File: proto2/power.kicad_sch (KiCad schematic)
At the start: 27 parts, among them Q15 2N7002, Q16 AO3401A

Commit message: Final layout for 0.2.0 and various BOM and minor schematic updates.
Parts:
- added R158: 1K, Resistor_SMD:R_0805_2012Metric, symbol Device:R_Small
- C52, C53, R149, R19, R20, R53, R54, R59: Config DNP -> (none); MPN (none) -> DNP
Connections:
- net at Q15.1 (G), R55.1, R56.1: now also R158.1
- new net +3V3: R158.2
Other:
- note added: "DNP: R149"
- note added: "DNP: R54 R59"
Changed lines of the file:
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@@
   (junction (at 97.79 44.45) (diameter 0) (color 0 0 0 0)
   )
+  (junction (at 80.01 130.81) (diameter 0) (color 0 0 0 0)
+  )
   (junction (at 100.33 44.45) (diameter 0) (color 0 0 0 0)
   )
@@
     (stroke (width 0) (type default) (color 0 0 0 0))
   )
+  (wire (pts (xy 80.01 123.19) (xy 80.01 130.81))
+    (stroke (width 0) (type default) (color 0 0 0 0))
+  )
   (wire (pts (xy 228.6 128.27) (xy 228.6 123.19))
     (stroke (width 0) (type default) (color 0 0 0 0))
@@
     (stroke (width 0) (type default) (color 0 0 0 0))
   )
+  (wire (pts (xy 68.58 123.19) (xy 68.58 121.92))
+    (stroke (width 0) (type default) (color 0 0 0 0))
+  )
   (wire (pts (xy 195.58 52.07) (xy 210.82 52.07))
     (stroke (width 0) (type default) (color 0 0 0 0))
@@
     (stroke (width 0) (type default) (color 0 0 0 0))
   )
-  (wire (pts (xy 77.47 130.81) (xy 81.28 130.81))
+  (wire (pts (xy 77.47 130.81) (xy 80.01 130.81))
     (stroke (width 0) (type default) (color 0 0 0 0))
   )
@@
     (stroke (width 0) (type default) (color 0 0 0 0))
   )
+  (wire (pts (xy 72.39 123.19) (xy 68.58 123.19))
+    (stroke (width 0) (type default) (color 0 0 0 0))
+  )
   (wire (pts (xy 128.27 54.61) (xy 143.51 54.61))
     (stroke (width 0) (type default) (color 0 0 0 0))
@@
     (stroke (width 0) (type default) (color 0 0 0 0))
   )
+  (wire (pts (xy 77.47 123.19) (xy 80.01 123.19))
+    (stroke (width 0) (type default) (color 0 0 0 0))
+  )
   (wire (pts (xy 76.2 52.07) (xy 76.2 54.61))
     (stroke (width 0) (type default) (color 0 0 0 0))
@@
     (stroke (width 0) (type default) (color 0 0 0 0))
   )
+  (wire (pts (xy 80.01 130.81) (xy 81.28 130.81))
+    (stroke (width 0) (type default) (color 0 0 0 0))
+  )
   (wire (pts (xy 86.36 138.43) (xy 91.44 138.43))
     (stroke (width 0) (type default) (color 0 0 0 0))
@@
   (wire (pts (xy 224.79 123.19) (xy 228.6 123.19))
     (stroke (width 0) (type default) (color 0 0 0 0))
+  )
+  (text "DNP:\nR149" (at 138.43 118.11 0)
+    (effects (font (size 1.27 1.27)) (justify left bottom))
   )
   (text "https://electronics.stackexchange.com/questions/19561/should-chassis-ground-be-attached-to-digital-ground"
     (at 302.26 116.84 0)
+    (effects (font (size 1.27 1.27)) (justify left bottom))
+  )
+  (text "DNP:\nR54\nR59" (at 180.34 137.16 0)
     (effects (font (size 1.27 1.27)) (justify left bottom))
   )
@@
       (effects (font (size 1.27 1.27)) hide)
     )
-    (property "Datasheet" "~" (id 3) (at 68.58 44.45 0)
+    (property "Datasheet" "https://datasheet.lcsc.com/lcsc/1810250922_Murata-Electronics-LQH32PN2R2NN0L_C86074.pdf" (id 3) (at 68.58 44.45 0)
       (effects (font (size 1.27 1.27)) hide)
     )
@@
       (effects (font (size 1.27 1.27)) hide)
     )
-    (property "Datasheet" "~" (id 3) (at 46.99 49.53 0)
+    (property "Datasheet" "https://datasheet.lcsc.com/lcsc/1810261813_Honor-Elec-VT1H331M1213_C94443.pdf" (id 3) (at 46.99 49.53 0)
       (effects (font (size 1.27 1.27)) hide)
     )
@@
       (effects (font (size 1.27 1.27)) hide)
     )
-    (property "Datasheet" "~" (id 3) (at 87.63 49.53 0)
+    (property "Datasheet" "https://datasheet.lcsc.com/lcsc/1810261813_Honor-Elec-VT1H331M1213_C94443.pdf" (id 3) (at 87.63 49.53 0)
       (effects (font (size 1.27 1.27)) hide)
     )
@@
       (effects (font (size 1.27 1.27)) hide)
     )
-    (property "Config" "DNP" (id 4) (at 210.82 45.72 0)
+    (property "Config" "" (id 4) (at 210.82 45.72 0)
+      (effects (font (size 1.27 1.27)) hide)
+    )
+    (property "MPN" "DNP" (id 5) (at 210.82 45.72 0)
       (effects (font (size 1.27 1.27)) hide)
     )
@@
       (effects (font (size 1.27 1.27)) hide)
     )
-    (property "Config" "DNP" (id 4) (at 210.82 57.15 0)
+    (property "Config" "" (id 4) (at 210.82 57.15 0)
+      (effects (font (size 1.27 1.27)) hide)
+    )
+    (property "MPN" "DNP" (id 5) (at 210.82 57.15 0)
       (effects (font (size 1.27 1.27)) hide)
     )
@@
       (effects (font (size 1.27 1.27)) hide)
     )
-    (property "Config" "DNP" (id 5) (at 234.95 114.3 90)
+    (property "Config" "" (id 5) (at 234.95 114.3 90)
+      (effects (font (size 1.27 1.27)) hide)
+    )
+    (property "MPN" "DNP" (id 6) (at 234.95 114.3 0)
       (effects (font (size 1.27 1.27)) hide)
     )
@@
       (effects (font (size 1.27 1.27)) hide)
     )
-    (property "Config" "DNP" (id 5) (at 222.25 123.19 0)
+    (property "Config" "" (id 5) (at 222.25 123.19 0)
+      (effects (font (size 1.27 1.27)) hide)
+    )
+    (property "MPN" "DNP" (id 6) (at 222.25 123.19 0)
       (effects (font (size 1.27 1.27)) hide)
     )
@@
       (effects (font (size 1.27 1.27)) hide)
     )
-    (property "Config" "DNP" (id 5) (at 234.95 123.19 0)
+    (property "Config" "" (id 5) (at 234.95 123.19 0)
+      (effects (font (size 1.27 1.27)) hide)
+    )
+    (property "MPN" "DNP" (id 6) (at 234.95 123.19 0)
       (effects (font (size 1.27 1.27)) hide)
     )
@@
       (effects (font (size 1.27 1.27)) hide)
     )
-    (property "Config" "DNP" (id 5) (at 135.89 123.19 0)
+    (property "Config" "" (id 5) (at 135.89 123.19 0)
+      (effects (font (size 1.27 1.27)) hide)
+    )
+    (property "MPN" "DNP" (id 6) (at 135.89 123.19 0)
       (effects (font (size 1.27 1.27)) hide)
     )
@@
     (pin "1")
   )
+  (symbol (lib_id "Device:R_Small") (at 74.93 123.19 270) (unit 1)
+    (in_bom yes) (on_board yes)
+    (property "Reference" "R158" (id 0) (at 74.93 118.2116 90))
+    (property "Value" "1K" (id 1) (at 74.93 120.523 90))
+    (property "Footprint" "Resistor_SMD:R_0805_2012Metric" (id 2) (at 74.93 123.19 0)
+      (effects (font (size 1.27 1.27)) hide)
+    )
+    (property "Datasheet" "https://datasheet.lcsc.com/lcsc/2110251730_UNI-ROYAL-Uniroyal-Elec-0805W8F1001T5E_C17513.pdf" (id 3) (at 74.93 123.19 0)
+      (effects (font (size 1.27 1.27)) hide)
+    )
+    (property "LCSC" "C17513" (id 4) (at 74.93 123.19 0)
+      (effects (font (size 1.27 1.27)) hide)
+    )
+    (property "MPN" "DNP" (id 5) (at 74.93 123.19 0)
+      (effects (font (size 1.27 1.27)) hide)
+    )
+    (pin "1")
+    (pin "2")
+  )
   (symbol (lib_id "power:+5VP") (at 135.89 129.54 180) (unit 1)
     (in_bom yes) (on_board yes) (fields_autoplaced)
@@
   (symbol (lib_id "power:+5V") (at 210.82 40.64 0) (unit 1)
     (in_bom yes) (on_board yes)
-    (property "Reference" "#PWR?" (id 0) (at 210.82 44.45 0)
+    (property "Reference" "#PWR0120" (id 0) (at 210.82 44.45 0)
       (effects (font (size 1.27 1.27)) hide)
     )
@@
     (pin "1")
   )
+  (symbol (lib_id "power:+3.3V") (at 68.58 121.92 0) (unit 1)
+    (in_bom yes) (on_board yes)
+    (property "Reference" "#PWR035" (id 0) (at 68.58 125.73 0)
+      (effects (font (size 1.27 1.27)) hide)
+    )
+    (property "Value" "+3.3V" (id 1) (at 68.961 117.5258 0))
+    (property "Footprint" "" (id 2) (at 68.58 121.92 0)
+      (effects (font (size 1.27 1.27)) hide)
+    )
+    (property "Datasheet" "" (id 3) (at 68.58 121.92 0)
+      (effects (font (size 1.27 1.27)) hide)
+    )
+    (pin "1")
+  )
   (symbol (lib_id "Transistor_FET:AO3401A") (at 118.11 123.19 0) (mirror x) (unit 1)
     (in_bom yes) (on_board yes) (fields_autoplaced)
@@
       (effects (font (size 1.27 1.27)) hide)
     )
-    (property "Config" "DNP" (id 5) (at 171.45 119.38 90)
+    (property "Config" "" (id 5) (at 171.45 119.38 90)
+      (effects (font (size 1.27 1.27)) hide)
+    )
+    (property "MPN" "DNP" (id 6) (at 171.45 119.38 0)
       (effects (font (size 1.27 1.27)) hide)
     )
@@
   (symbol (lib_id "power:+5V") (at 168.91 35.56 0) (unit 1)
     (in_bom yes) (on_board yes)
-    (property "Reference" "#PWR?" (id 0) (at 168.91 39.37 0)
+    (property "Reference" "#PWR0108" (id 0) (at 168.91 39.37 0)
       (effects (font (size 1.27 1.27)) hide)
     )
@@
       (effects (font (size 1.27 1.27)) hide)
     )
-    (property "Config" "DNP" (id 5) (at 171.45 127 90)
-      (effects (font (size 1.27 1.27)) hide)
-    )
+    (property "Config" "" (id 5) (at 171.45 127 90)
+      (effects (font (size 1.27 1.27)) hide)
+    )
+    (property "MPN" "DNP" (id 6) (at 171.45 127 0)
+      (effects (font (size 1.27 1.27)) hide)
+    )

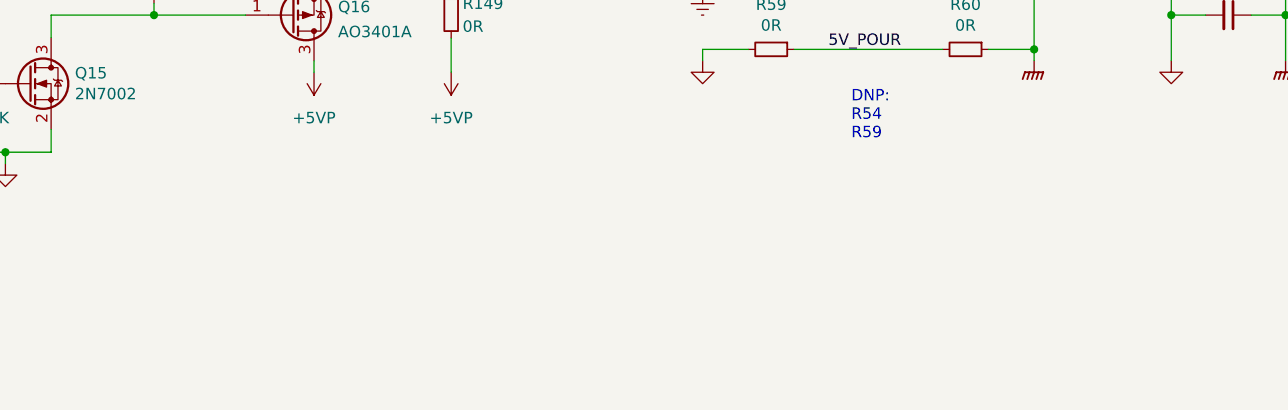
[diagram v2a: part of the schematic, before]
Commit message: Rearranged GPIO around the boot pins.
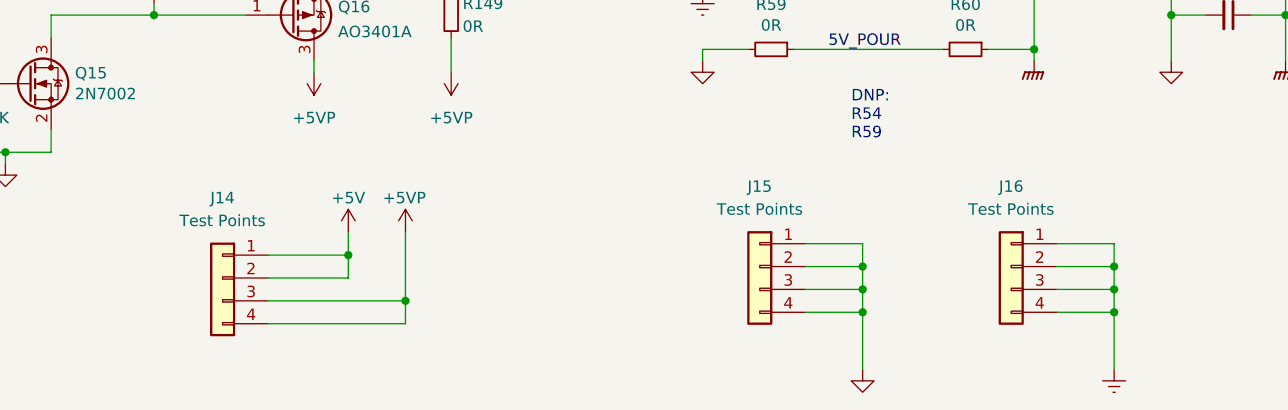
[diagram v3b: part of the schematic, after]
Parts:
- added J14, J15, J16: Test Points, Connector_PinHeader_2.54mm:PinHeader_1x04_P2.54mm_Vertical, symbol Connector_Generic:Conn_01x04
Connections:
- net +5V: now also J14.1 (Pin_1), J14.2 (Pin_2)
- net +5VP: now also J14.3 (Pin_3), J14.4 (Pin_4)
- net GND-PWR: now also J16.1 (Pin_1), J16.2 (Pin_2), J16.3 (Pin_3), J16.4 (Pin_4)
- net GND-SIG: now also J15.1 (Pin_1), J15.2 (Pin_2), J15.3 (Pin_3), J15.4 (Pin_4)

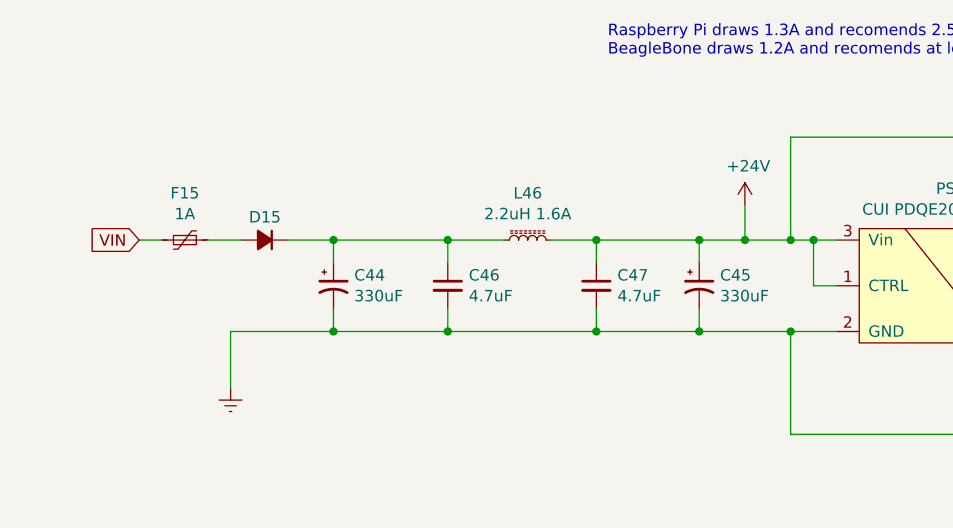
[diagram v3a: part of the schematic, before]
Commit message: Added larger fuse for 24V, replaced main polarity diode, and relayed out board to fit new components.
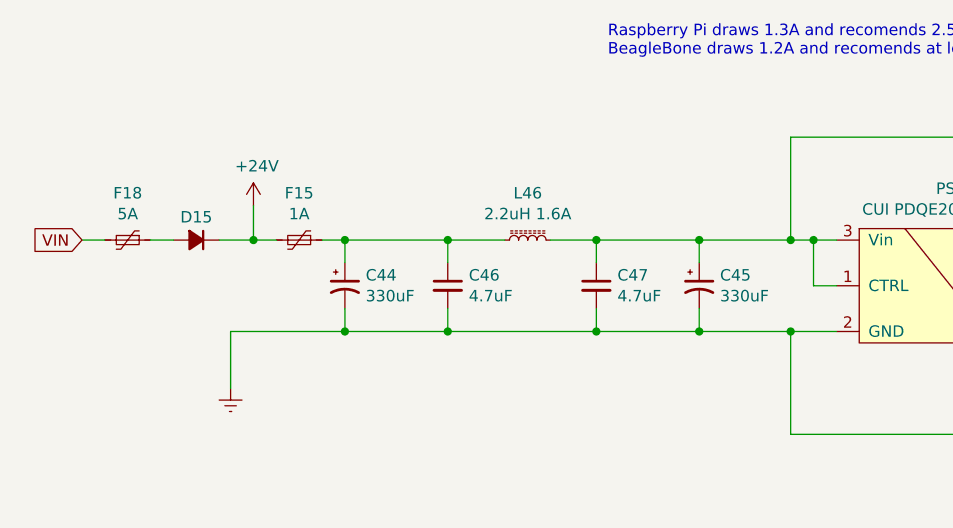
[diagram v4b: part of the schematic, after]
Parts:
- added F18: 5A, JLCPCB:F_2920, symbol Device:Polyfuse_Small
- D15: footprint Diode_SMD:D_SOD-123F -> Diode_SMD:D_SMC; LCSC C64898 -> C335615; Manufacturer MDD -> Vishay; Part Number SM4007PL -> S5JHE3_A/I
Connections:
- net +24V: now also D15.1 (K), F15.2; no longer C43.2, C45.1, C47.1, L46.2, PS1.1 (CTRL), PS1.3 (Vin)
- net VIN: now also F18.2; no longer F15.2
- net at C44.1, C46.1, L46.1: now also F15.1; no longer D15.1 (K)
- net at D15.2 (A): now also F18.1; no longer F15.1
- new net: C43.2, C45.1, C47.1, L46.2, PS1.1 (CTRL), PS1.3 (Vin)
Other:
- moved on the sheet: C44, D15, F15

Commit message: Updated PTC sizes so they will not trip with typical current draw.
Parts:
- F15: footprint Resistor_SMD:R_1206_3216Metric -> JLCPCB:F_2920; LCSC C70077 -> C409807
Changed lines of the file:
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@@
     (property "Reference" "F15" (id 0) (at 43.18 39.243 90))
     (property "Value" "1A" (id 1) (at 43.18 41.5544 90))
-    (property "Footprint" "Resistor_SMD:R_1206_3216Metric" (id 2) (at 38.1 45.72 0)
+    (property "Footprint" "JLCPCB:F_2920" (id 2) (at 38.1 45.72 0)
       (effects (font (size 1.27 1.27)) (justify left) hide)
     )
-    (property "Datasheet" "https://datasheet.lcsc.com/lcsc/1809211126_TECHFUSE-nSMD050-33V_C70077.pdf" (id 3) (at 43.18 44.45 0)
+    (property "Datasheet" "https://datasheet.lcsc.com/lcsc/1912111437_Jinrui-Electronic-Materials-Co--JK-SMD100L_C409807.pdf" (id 3) (at 43.18 44.45 0)
       (effects (font (size 1.27 1.27)) hide)
     )
-    (property "LCSC" "C70077" (id 4) (at 43.18 44.45 0)
+    (property "LCSC" "C409807" (id 4) (at 43.18 44.45 0)
       (effects (font (size 1.27 1.27)) hide)
     )

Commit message: Changed revision on schematic to 0.3.0.
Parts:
- J14, J15, J16, PS1: now left out of the parts list
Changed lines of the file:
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@@
   (title_block
     (title "Greenhouse 2.0 IO Board")
-    (date "2022-06-07")
-    (rev "0.2.1")
+    (date "2022-07-26")
+    (rev "0.3.0")
     (company "Langhe Greenhaus")
     (comment 1 "Langhe Part Number: 240000")
@@
   )
   (symbol (lib_id "BCR:CUI_PDQE20_ISOLATED_DCDC") (at 115.57 49.53 0) (unit 1)
-    (in_bom yes) (on_board yes)
+    (in_bom no) (on_board yes)
     (property "Reference" "PS1" (id 0) (at 115.57 38.735 0))
     (property "Value" "CUI PDQE20-Q24-S5-D" (id 1) (at 115.57 41.0464 0))
@@
   )
   (symbol (lib_id "Connector_Generic:Conn_01x04") (at 170.18 151.13 0) (mirror y) (unit 1)
-    (in_bom yes) (on_board yes) (fields_autoplaced)
+    (in_bom no) (on_board yes) (fields_autoplaced)
     (property "Reference" "J15" (id 0) (at 170.18 142.24 0))
     (property "Value" "Test Points" (id 1) (at 170.18 144.78 0))
@@
   )
   (symbol (lib_id "Connector_Generic:Conn_01x04") (at 110.49 152.4 0) (mirror y) (unit 1)
-    (in_bom yes) (on_board yes) (fields_autoplaced)
+    (in_bom no) (on_board yes) (fields_autoplaced)
     (property "Reference" "J14" (id 0) (at 110.49 143.51 0))
     (property "Value" "Test Points" (id 1) (at 110.49 146.05 0))
@@
   )
   (symbol (lib_id "Connector_Generic:Conn_01x04") (at 198.12 151.13 0) (mirror y) (unit 1)
-    (in_bom yes) (on_board yes) (fields_autoplaced)
+    (in_bom no) (on_board yes) (fields_autoplaced)
     (property "Reference" "J16" (id 0) (at 198.12 142.24 0))
     (property "Value" "Test Points" (id 1) (at 198.12 144.78 0))

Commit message: Updated part number for F15 and D15.
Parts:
- D15: LCSC C335615 -> C437690; Manufacturer Vishay -> Shandong Jingdao Microelectronics; Part Number S5JHE3_A/I -> S3GC
- F15: LCSC C409807 -> C262039; MPN (none) -> TLC-LSMD100; Manufacturer (none) -> TLC Electronic
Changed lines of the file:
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@@
       (effects (font (size 1.27 1.27)) (justify left) hide)
     )
-    (property "Datasheet" "https://datasheet.lcsc.com/lcsc/1912111437_Jinrui-Electronic-Materials-Co--JK-SMD100L_C409807.pdf" (id 3) (at 43.18 44.45 0)
+    (property "Datasheet" "https://datasheet.lcsc.com/lcsc/1809292114_TLC-Electronic-TLC-LSMD100_C262039.pdf" (id 3) (at 43.18 44.45 0)
       (effects (font (size 1.27 1.27)) hide)
     )
-    (property "LCSC" "C409807" (id 4) (at 43.18 44.45 0)
+    (property "LCSC" "C262039" (id 4) (at 43.18 44.45 0)
+      (effects (font (size 1.27 1.27)) hide)
+    )
+    (property "MPN" "TLC-LSMD100" (id 5) (at 43.18 44.45 0)
+      (effects (font (size 1.27 1.27)) hide)
+    )
+    (property "Manufacturer" "TLC Electronic" (id 6) (at 43.18 44.45 0)
       (effects (font (size 1.27 1.27)) hide)
     )
@@
       (effects (font (size 1.27 1.27)) hide)
     )
-    (property "Datasheet" "https://datasheet.lcsc.com/lcsc/1912111437_Vishay-Intertech-S5JHE3-A-I_C335615.pdf" (id 3) (at 31.75 44.45 90)
+    (property "Datasheet" "https://datasheet.lcsc.com/lcsc/1912111437_Shandong-Jingdao-Microelectronics-S3GC_C437690.pdf" (id 3) (at 31.75 44.45 90)
       (effects (font (size 1.27 1.27)) hide)
     )
-    (property "LCSC" "C335615" (id 4) (at 31.75 44.45 0)
+    (property "LCSC" "C437690" (id 4) (at 31.75 44.45 0)
       (effects (font (size 1.27 1.27)) hide)
     )
-    (property "Manufacturer" "Vishay" (id 5) (at 31.75 44.45 0)
+    (property "Manufacturer" "Shandong Jingdao Microelectronics" (id 5) (at 31.75 44.45 0)
       (effects (font (size 1.27 1.27)) hide)
     )
-    (property "Part Number" "S5JHE3_A/I" (id 6) (at 31.75 44.45 0)
+    (property "Part Number" "S3GC" (id 6) (at 31.75 44.45 0)
       (effects (font (size 1.27 1.27)) hide)
     )

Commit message: Updated F15,D15,U1-14 to parts in stock at JLC. Updated U1-14 footprints to more common size.
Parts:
- F18: Part Nmber SHV2920P500-30-AA -> (none); Part Number (none) -> SHV2920P500-30-AA
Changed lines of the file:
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@@
   (title_block
     (title "Greenhouse 2.0 IO Board")
-    (date "2022-07-26")
-    (rev "0.3.0")
+    (date "2022-08-04")
+    (rev "0.3.1")
     (company "Langhe Greenhaus")
     (comment 1 "Langhe Part Number: 240000")
@@
       (effects (font (size 1.27 1.27)) hide)
     )
-    (property "Part Nmber" "SHV2920P500-30-AA" (id 6) (at 24.13 44.45 90)
-      (effects (font (size 1.27 1.27)) hide)
-    )
+    (property "Part Number" "SHV2920P500-30-AA" (id 6) (at 24.13 44.45 0)
+      (effects (font (size 1.27 1.27)) hide)
+    )
